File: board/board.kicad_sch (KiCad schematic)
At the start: 3 parts, among them J1 004_BASE-T_CT_2x3, J2 013_PoE_rectified

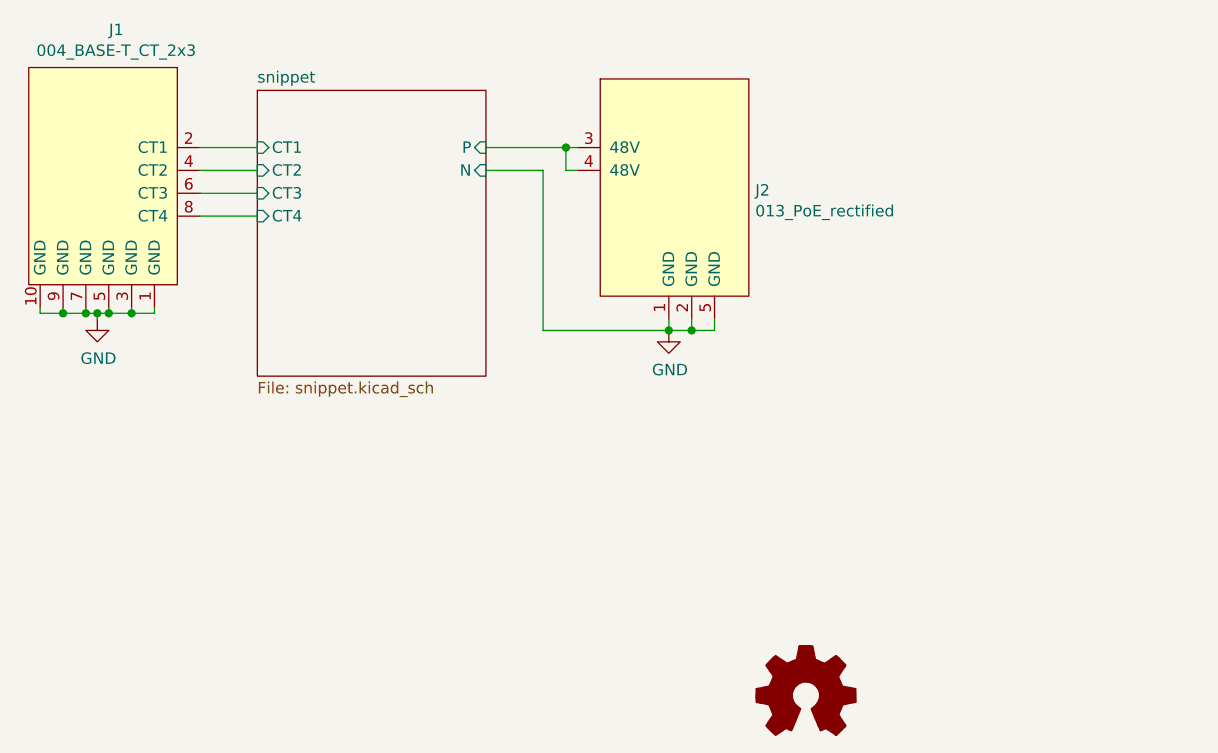
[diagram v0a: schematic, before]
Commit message: updated connectors, changed mosfets and added enable resistors
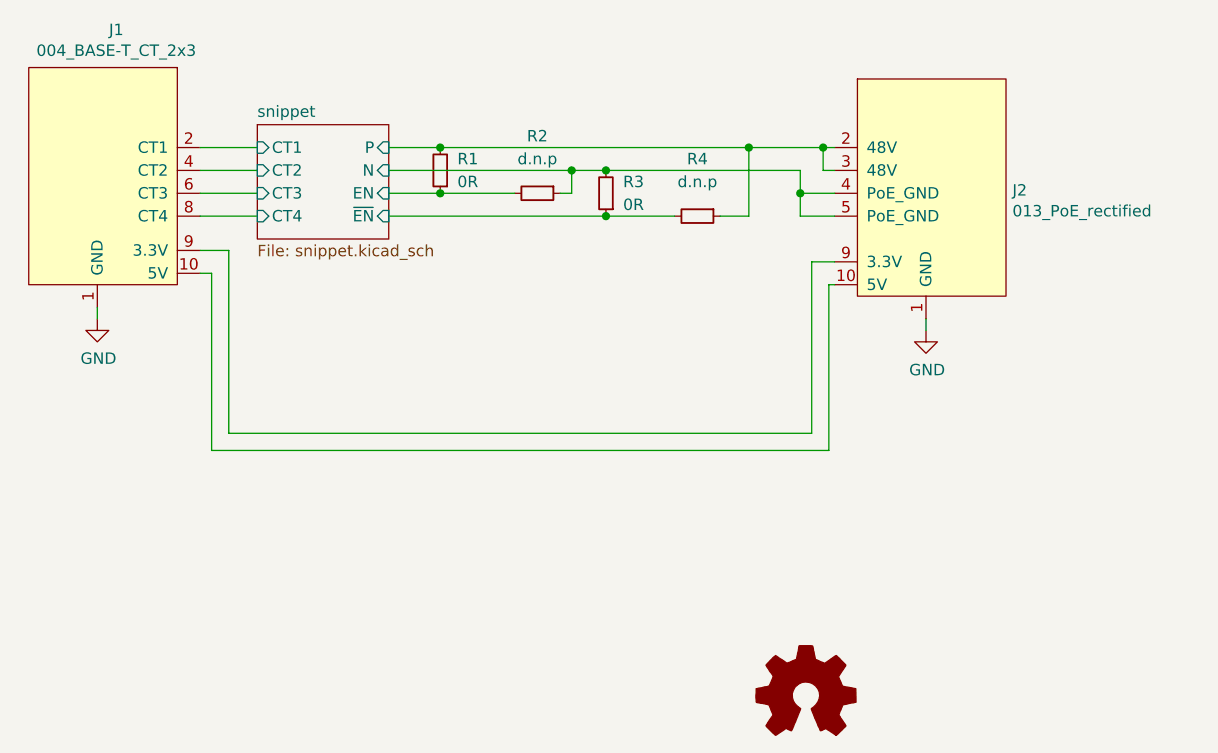
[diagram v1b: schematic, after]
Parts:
- added R1, R3: 0R, Resistor_SMD:R_0603_1608Metric, symbol Device:R_Small
- added R2, R4: d.n.p, Resistor_SMD:R_0603_1608Metric, symbol Device:R_Small
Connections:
- net GND: no longer J1.10 (GND), J1.3 (GND), J1.5 (GND), J1.7 (GND), J1.9 (GND), J2.2 (GND), J2.5 (GND)
- net snippet/P: now also J2.2 (48V), R1.2, R4.1; no longer J2.4 (48V)
- new net: J1.10 (5V), J2.10 (5V)
- new net: J1.9 (3.3V), J2.9 (3.3V)
- new net snippet/EN: R1.1, R2.2
- new net snippet/N: J2.4 (PoE_GND), J2.5 (PoE_GND), R2.1, R3.2
- new net snippet/~{EN}: R3.1, R4.2
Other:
- sheet snippet ports: added EN, ~{EN}; removed none

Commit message: added enable input from downstream
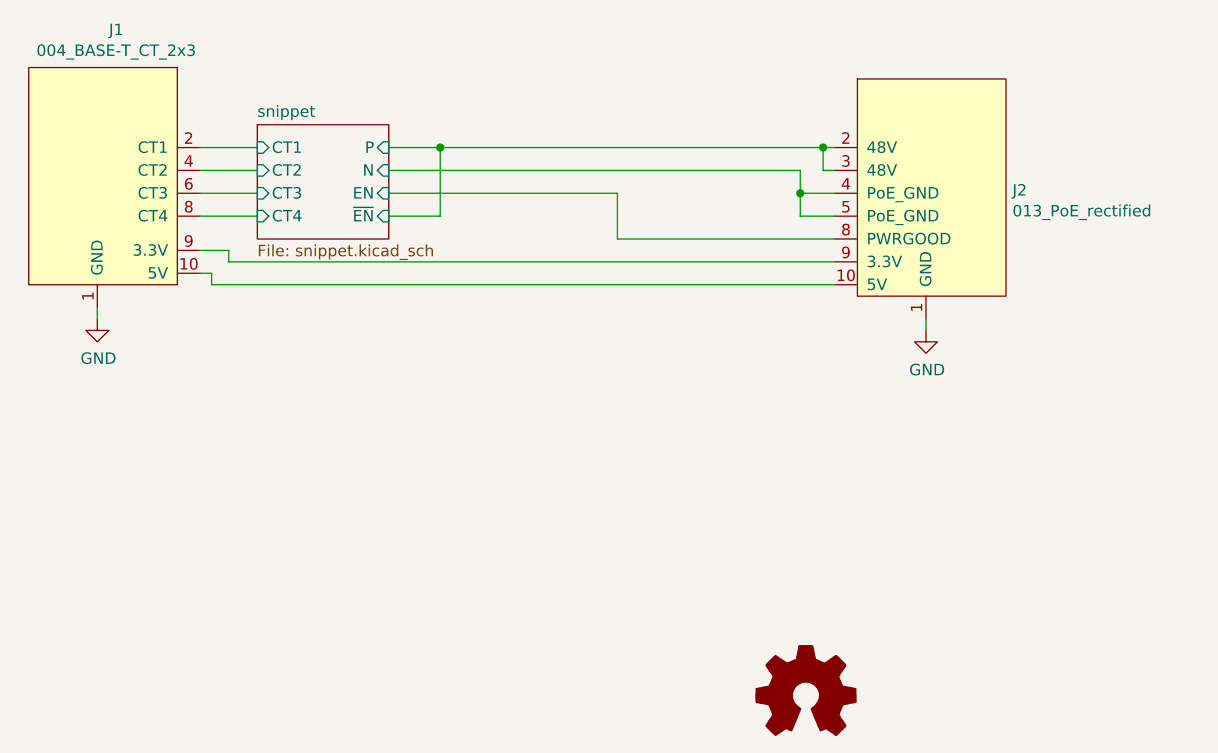
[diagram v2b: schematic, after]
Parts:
- removed R1, R3: 0R, Resistor_SMD:R_0603_1608Metric, symbol Device:R_Small
- removed R2, R4: d.n.p, Resistor_SMD:R_0603_1608Metric, symbol Device:R_Small
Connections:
- net snippet/EN: now also J2.8 (PWRGOOD)
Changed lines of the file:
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@@
 (kicad_sch (version 20211123) (generator eeschema)
   (paper "A4")
-  (junction (at 165.735 72.39) (diameter 0) (color 0 0 0 0)
-  )
   (junction (at 189.865 69.85) (diameter 0) (color 0 0 0 0)
   )
-  (junction (at 147.32 74.93) (diameter 0) (color 0 0 0 0)
+  (junction (at 187.325 74.93) (diameter 0) (color 0 0 0 0)
   )
   (junction (at 147.32 69.85) (diameter 0) (color 0 0 0 0)
   )
-  (junction (at 187.325 74.93) (diameter 0) (color 0 0 0 0)
-  )
-  (junction (at 165.735 77.47) (diameter 0) (color 0 0 0 0)
-  )
-  (junction (at 161.925 72.39) (diameter 0) (color 0 0 0 0)
-  )
-  (junction (at 181.61 69.85) (diameter 0) (color 0 0 0 0)
-  )
-  (wire (pts (xy 147.32 69.85) (xy 181.61 69.85))
+  (wire (pts (xy 141.605 69.85) (xy 147.32 69.85))
+    (stroke (width 0) (type default) (color 0 0 0 0))
+  )
+  (wire (pts (xy 141.605 72.39) (xy 187.325 72.39))
     (stroke (width 0) (type default) (color 0 0 0 0))
   )
@@
     (stroke (width 0) (type default) (color 0 0 0 0))
   )
-  (wire (pts (xy 161.925 72.39) (xy 165.735 72.39))
-    (stroke (width 0) (type default) (color 0 0 0 0))
-  )
-  (wire (pts (xy 188.595 82.55) (xy 188.595 101.6))
-    (stroke (width 0) (type default) (color 0 0 0 0))
-  )
-  (wire (pts (xy 178.435 77.47) (xy 181.61 77.47))
+  (wire (pts (xy 167.005 74.93) (xy 167.005 80.01))
+    (stroke (width 0) (type default) (color 0 0 0 0))
+  )
+  (wire (pts (xy 147.32 69.85) (xy 189.865 69.85))
+    (stroke (width 0) (type default) (color 0 0 0 0))
+  )
+  (wire (pts (xy 167.005 80.01) (xy 191.135 80.01))
     (stroke (width 0) (type default) (color 0 0 0 0))
   )
@@
     (stroke (width 0) (type default) (color 0 0 0 0))
   )
-  (wire (pts (xy 181.61 69.85) (xy 181.61 77.47))
-    (stroke (width 0) (type default) (color 0 0 0 0))
-  )
   (wire (pts (xy 120.65 74.93) (xy 127 74.93))
     (stroke (width 0) (type default) (color 0 0 0 0))
   )
-  (wire (pts (xy 165.735 77.47) (xy 173.355 77.47))
-    (stroke (width 0) (type default) (color 0 0 0 0))
-  )
-  (wire (pts (xy 141.605 72.39) (xy 161.925 72.39))
+  (wire (pts (xy 141.605 77.47) (xy 147.32 77.47))
     (stroke (width 0) (type default) (color 0 0 0 0))
   )
@@
     (stroke (width 0) (type default) (color 0 0 0 0))
   )
-  (wire (pts (xy 165.735 72.39) (xy 187.325 72.39))
-    (stroke (width 0) (type default) (color 0 0 0 0))
-  )
-  (wire (pts (xy 161.925 74.93) (xy 161.925 72.39))
-    (stroke (width 0) (type default) (color 0 0 0 0))
-  )
-  (wire (pts (xy 141.605 74.93) (xy 147.32 74.93))
+  (wire (pts (xy 141.605 74.93) (xy 167.005 74.93))
     (stroke (width 0) (type default) (color 0 0 0 0))
   )
@@
     (stroke (width 0) (type default) (color 0 0 0 0))
   )
-  (wire (pts (xy 188.595 101.6) (xy 123.825 101.6))
-    (stroke (width 0) (type default) (color 0 0 0 0))
-  )
   (wire (pts (xy 187.325 72.39) (xy 187.325 74.93))
     (stroke (width 0) (type default) (color 0 0 0 0))
   )
-  (wire (pts (xy 160.655 74.93) (xy 161.925 74.93))
-    (stroke (width 0) (type default) (color 0 0 0 0))
-  )
   (wire (pts (xy 189.865 72.39) (xy 189.865 69.85))
     (stroke (width 0) (type default) (color 0 0 0 0))
   )
-  (wire (pts (xy 190.5 85.09) (xy 191.135 85.09))
-    (stroke (width 0) (type default) (color 0 0 0 0))
-  )
-  (wire (pts (xy 147.32 74.93) (xy 155.575 74.93))
-    (stroke (width 0) (type default) (color 0 0 0 0))
-  )
-  (wire (pts (xy 190.5 103.505) (xy 190.5 85.09))
+  (wire (pts (xy 121.92 85.09) (xy 191.135 85.09))
     (stroke (width 0) (type default) (color 0 0 0 0))
   )
@@
     (stroke (width 0) (type default) (color 0 0 0 0))
   )
-  (wire (pts (xy 121.92 103.505) (xy 190.5 103.505))
-    (stroke (width 0) (type default) (color 0 0 0 0))
-  )
   (wire (pts (xy 123.825 81.28) (xy 120.65 81.28))
     (stroke (width 0) (type default) (color 0 0 0 0))
   )
-  (wire (pts (xy 191.135 82.55) (xy 188.595 82.55))
-    (stroke (width 0) (type default) (color 0 0 0 0))
-  )
-  (wire (pts (xy 123.825 101.6) (xy 123.825 81.28))
-    (stroke (width 0) (type default) (color 0 0 0 0))
-  )
-  (wire (pts (xy 181.61 69.85) (xy 189.865 69.85))
+  (wire (pts (xy 123.825 82.55) (xy 191.135 82.55))
+    (stroke (width 0) (type default) (color 0 0 0 0))
+  )
+  (wire (pts (xy 123.825 82.55) (xy 123.825 81.28))
+    (stroke (width 0) (type default) (color 0 0 0 0))
+  )
+  (wire (pts (xy 147.32 69.85) (xy 147.32 77.47))
     (stroke (width 0) (type default) (color 0 0 0 0))
   )
@@
     (stroke (width 0) (type default) (color 0 0 0 0))
   )
-  (wire (pts (xy 141.605 69.85) (xy 147.32 69.85))
-    (stroke (width 0) (type default) (color 0 0 0 0))
-  )
   (wire (pts (xy 120.65 83.82) (xy 121.92 83.82))
     (stroke (width 0) (type default) (color 0 0 0 0))
   )
-  (wire (pts (xy 121.92 83.82) (xy 121.92 103.505))
-    (stroke (width 0) (type default) (color 0 0 0 0))
-  )
-  (wire (pts (xy 141.605 77.47) (xy 165.735 77.47))
+  (wire (pts (xy 121.92 83.82) (xy 121.92 85.09))
     (stroke (width 0) (type default) (color 0 0 0 0))
   )
@@
     (pin "4")
     (pin "5")
+    (pin "8")
     (pin "9")
-  )
-  (symbol (lib_id "Device:R_Small") (at 175.895 77.47 270) (unit 1)
-    (in_bom yes) (on_board yes) (fields_autoplaced)
-    (property "Reference" "R4" (id 0) (at 175.895 71.12 90))
-    (property "Value" "d.n.p" (id 1) (at 175.895 73.66 90))
-    (property "Footprint" "Resistor_SMD:R_0603_1608Metric" (id 2) (at 175.895 77.47 0)
-      (effects (font (size 1.27 1.27)) hide)
-    )
-    (property "Datasheet" "~" (id 3) (at 175.895 77.47 0)
-      (effects (font (size 1.27 1.27)) hide)
-    )
-    (pin "1")
-    (pin "2")
-  )
-  (symbol (lib_id "Device:R_Small") (at 147.32 72.39 180) (unit 1)
-    (in_bom yes) (on_board yes) (fields_autoplaced)
-    (property "Reference" "R1" (id 0) (at 149.225 71.1199 0)
-      (effects (font (size 1.27 1.27)) (justify right))
-    )
-    (property "Value" "0R" (id 1) (at 149.225 73.6599 0)
-      (effects (font (size 1.27 1.27)) (justify right))
-    )
-    (property "Footprint" "Resistor_SMD:R_0603_1608Metric" (id 2) (at 147.32 72.39 0)
-      (effects (font (size 1.27 1.27)) hide)
-    )
-    (property "Datasheet" "~" (id 3) (at 147.32 72.39 0)
-      (effects (font (size 1.27 1.27)) hide)
-    )
-    (pin "1")
-    (pin "2")
-  )
-  (symbol (lib_id "Device:R_Small") (at 158.115 74.93 270) (unit 1)
-    (in_bom yes) (on_board yes) (fields_autoplaced)
-    (property "Reference" "R2" (id 0) (at 158.115 68.58 90))
-    (property "Value" "d.n.p" (id 1) (at 158.115 71.12 90))
-    (property "Footprint" "Resistor_SMD:R_0603_1608Metric" (id 2) (at 158.115 74.93 0)
-      (effects (font (size 1.27 1.27)) hide)
-    )
-    (property "Datasheet" "~" (id 3) (at 158.115 74.93 0)
-      (effects (font (size 1.27 1.27)) hide)
-    )
-    (pin "1")
-    (pin "2")
-  )
-  (symbol (lib_id "Device:R_Small") (at 165.735 74.93 180) (unit 1)
-    (in_bom yes) (on_board yes) (fields_autoplaced)
-    (property "Reference" "R3" (id 0) (at 167.64 73.6599 0)
-      (effects (font (size 1.27 1.27)) (justify right))
-    )
-    (property "Value" "0R" (id 1) (at 167.64 76.1999 0)
-      (effects (font (size 1.27 1.27)) (justify right))
-    )
-    (property "Footprint" "Resistor_SMD:R_0603_1608Metric" (id 2) (at 165.735 74.93 0)
-      (effects (font (size 1.27 1.27)) hide)
-    )
-    (property "Datasheet" "~" (id 3) (at 165.735 74.93 0)
-      (effects (font (size 1.27 1.27)) hide)
-    )
-    (pin "1")
-    (pin "2")
   )
   (sheet (at 127 67.31) (size 14.605 12.7) (fields_autoplaced)
@@
       (reference "Q8") (unit 1) (value "PSMN075-100MSEX") (footprint "Package_TO_SOT_SMD:LFPAK33")
     )
-    (path "/620c2cae-5d7f-489c-ae7a-3549312a4159"
-      (reference "R1") (unit 1) (value "0R") (footprint "Resistor_SMD:R_0603_1608Metric")
-    )
-    (path "/6d245bb6-6dba-41cf-982a-c7911c26838d"
-      (reference "R2") (unit 1) (value "d.n.p") (footprint "Resistor_SMD:R_0603_1608Metric")
-    )
-    (path "/b2627d30-bacc-4022-96cb-29a47c7e3f6d"
-      (reference "R3") (unit 1) (value "0R") (footprint "Resistor_SMD:R_0603_1608Metric")
-    )
-    (path "/35bee981-9437-4dff-adaa-d304d2bd2cf8"
-      (reference "R4") (unit 1) (value "d.n.p") (footprint "Resistor_SMD:R_0603_1608Metric")
-    )
     (path "/00000000-0000-0000-0000-00006031befe/00000000-0000-0000-0000-000060323155"
